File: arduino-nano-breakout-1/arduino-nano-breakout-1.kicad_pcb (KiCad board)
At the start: 2 copper layers, 7 x 7 mm, 4 parts, among them J1 PJ-002A, J2 Conn_01x03_Male, J4 Conn_01x08_Male

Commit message: move
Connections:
- J4 pad 2: Net-(A1-Pad27) -> Net-(J1-Pad1)
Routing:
- net Net-(J1-Pad1): track 14.5 -> 51.3 mm
- net GND: track 65.4 -> 80.5 mm, vias 1 -> 2
- net Net-(A1-Pad27): track 42.7 -> 48.2 mm
- net Net-(A1-Pad30): track 52.1 -> 55.2 mm

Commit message: final piece?
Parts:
- added JP1: SolderJumper_3_Open, Jumper:SolderJumper-3_P1.3mm_Open_Pad1.0x1.5mm, F.Cu at (134.6, 77.5)
- added JP2: SolderJumper_3_Open, Jumper:SolderJumper-3_P1.3mm_Open_Pad1.0x1.5mm, F.Cu at (134.6, 85.1)
- added JP3: SolderJumper_3_Open, Jumper:SolderJumper-3_P1.3mm_Open_Pad1.0x1.5mm, F.Cu at (134.6, 92.7)
- added JP4: SolderJumper_3_Open, Jumper:SolderJumper-3_P1.3mm_Open_Pad1.0x1.5mm, F.Cu at (134.6, 100.3)
- J1: footprint CUI_PJ-002A -> SS_connectors:CUI_PJ-002A
- moved J4 2.29 mm to (157.5, 79.4)
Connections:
- A1 pad 1: Net-(A1-Pad1) -> (no net)
- A1 pad 10: Net-(A1-Pad10) -> (no net)
- A1 pad 11: Net-(A1-Pad11) -> (no net)
- A1 pad 14: Net-(A1-Pad14) -> (no net)
- A1 pad 15: Net-(A1-Pad15) -> (no net)
- A1 pad 16: Net-(A1-Pad16) -> (no net)
- A1 pad 17: Net-(A1-Pad17) -> (no net)
- A1 pad 18: Net-(A1-Pad18) -> (no net)
- A1 pad 19: Net-(A1-Pad19) -> (no net)
- A1 pad 2: Net-(A1-Pad2) -> (no net)
- A1 pad 20: Net-(A1-Pad20) -> (no net)
- A1 pad 23: Net-(A1-Pad23) -> (no net)
- A1 pad 26: Net-(A1-Pad26) -> (no net)
- A1 pad 28: Net-(A1-Pad28) -> (no net)
- A1 pad 3: Net-(A1-Pad3) -> (no net)
- A1 pad 7: Net-(A1-Pad7) -> (no net)
- J1 pad 3: Net-(J1-Pad3) -> (no net)
- J4 pad 1: GND -> Net-(J4-Pad1)
- J4 pad 2: Net-(J1-Pad1) -> Net-(J4-Pad2)
- J4 pad 3: IO2 -> Net-(J4-Pad3)
- J4 pad 4: IO3 -> Net-(J4-Pad4)
- J4 pad 5: IO5 -> IO9
- J4 pad 6: IO6 -> IO10
- J4 pad 7: IO9 -> GND
- J4 pad 8: IO10 -> Net-(J1-Pad1)
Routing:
- net GND: track 80.5 -> 18.9 mm, vias 2 -> 4
- net Net-(J1-Pad1): track 51.3 -> 15.4 mm, vias 0 -> 2
- net Net-(A1-Pad21): track 0.00 -> 31.5 mm, vias 0 -> 1
- net Net-(J4-Pad4): track 0.00 -> 30.2 mm, vias 0 -> 1
- net Net-(J4-Pad3): track 0.00 -> 26.3 mm, vias 0 -> 1
- net Net-(J4-Pad1): track 0.00 -> 26.2 mm, vias 0 -> 1
- net IO5: track 29.3 -> 5.09 mm, vias 0 -> 1
- net Net-(J4-Pad2): track 0.00 -> 24.2 mm, vias 0 -> 1
- net Net-(A1-Pad25): track 0.00 -> 23.7 mm, vias 0 -> 1
- net Net-(A1-Pad22): track 0.00 -> 22.5 mm, vias 0 -> 1
- net IO3: track 28.2 -> 6.52 mm, vias 0 -> 1
- net IO6: track 29.3 -> 8.31 mm, vias 0 -> 1
- net Net-(A1-Pad27): track 48.2 -> 31.4 mm
- net IO2: track 28.2 -> 11.5 mm, vias 0 -> 1
- net Net-(A1-Pad30): track 55.2 -> 44.5 mm
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- added copper zone on B.Cu, net GND
- added copper zone on B.Cu, net Net-(J1-Pad1)
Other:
- board size 7 x 7 mm -> 37.5 x 48.9 mm

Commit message: VDD filtering capacitors
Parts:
- added C1: 100nF, Capacitor_SMD:C_0805_2012Metric, F.Cu at (148.3, 77.5)
- added C2: 100nF, Capacitor_SMD:C_0805_2012Metric, F.Cu at (149.2, 81.6)
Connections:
- A1 pad 1: (no net) -> Net-(A1-Pad1)
- A1 pad 10: (no net) -> Net-(A1-Pad10)
- A1 pad 11: (no net) -> Net-(A1-Pad11)
- A1 pad 14: (no net) -> Net-(A1-Pad14)
- A1 pad 15: (no net) -> Net-(A1-Pad15)
- A1 pad 16: (no net) -> Net-(A1-Pad16)
- A1 pad 17: (no net) -> Net-(A1-Pad17)
- A1 pad 18: (no net) -> Net-(A1-Pad18)
- A1 pad 19: (no net) -> Net-(A1-Pad19)
- A1 pad 2: (no net) -> Net-(A1-Pad2)
- A1 pad 20: (no net) -> Net-(A1-Pad20)
- A1 pad 23: (no net) -> Net-(A1-Pad23)
- A1 pad 26: (no net) -> Net-(A1-Pad26)
- A1 pad 28: (no net) -> Net-(A1-Pad28)
- A1 pad 3: (no net) -> Net-(A1-Pad3)
- A1 pad 7: (no net) -> Net-(A1-Pad7)
- J1 pad 3: (no net) -> Net-(J1-Pad3)
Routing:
- net GND: track 18.9 -> 21.5 mm, vias 4 -> 6
- net Net-(A1-Pad27): track 31.4 -> 32.7 mm

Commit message: Add silks
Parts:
- moved C2 1.82 mm to (150.5, 82.9)
- renumbered JP1 to IO_2, JP2 to IO_3, JP3 to IO_5, JP4 to IO_6
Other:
- board text added: "A2"
- board text added: "A3"
- board text added: "A5"
- board text added: "A6"
- board text added: "D2"
- board text added: "D3"
- board text added: "D5"
- board text added: "D6"
- board text added: "GND"
- board text added: "IO_10"
- board text added: "IO_2"
- board text added: "IO_3"
- board text added: "IO_5"
- board text added: "IO_6"
- board text added: "IO_9"
- board text added: "Vout"
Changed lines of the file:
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@@
   (general
     (thickness 1.6)
-    (drawings 4)
-    (tracks 149)
+    (drawings 20)
+    (tracks 150)
     (zones 0)
     (modules 10)
@@
     (tags "solder jumper open")
     (attr virtual)
-    (fp_text reference JP1 (at 0 -1.8 270) (layer F.SilkS)
+    (fp_text reference IO_2 (at 0 -1.8 270) (layer F.SilkS)
       (effects (font (size 1 1) (thickness 0.15)))
     )
@@
     (tags "solder jumper open")
     (attr virtual)
-    (fp_text reference JP2 (at 0 -1.8 270) (layer F.SilkS)
+    (fp_text reference IO_3 (at 0 -1.8 270) (layer F.SilkS)
       (effects (font (size 1 1) (thickness 0.15)))
     )
@@
     (tags "solder jumper open")
     (attr virtual)
-    (fp_text reference JP3 (at 0 -1.8 270) (layer F.SilkS)
+    (fp_text reference IO_5 (at 0 -1.8 270) (layer F.SilkS)
       (effects (font (size 1 1) (thickness 0.15)))
     )
@@
     (tags "solder jumper open")
     (attr virtual)
-    (fp_text reference JP4 (at 0 -1.8 270) (layer F.SilkS)
+    (fp_text reference IO_6 (at 0 -1.8 270) (layer F.SilkS)
       (effects (font (size 1 1) (thickness 0.15)))
     )
@@
   )
   (module Capacitor_SMD:C_0805_2012Metric (layer F.Cu)
-    (at 149.225 81.5825 90)
+    (at 150.495 82.8825 90)
     (descr "Capacitor SMD 0805 (2012 Metric), square (rectangular) end terminal, IPC_7351 nominal, (Body size source: https://docs.google.com/spreadsheets/d/1BsfQQcO9C6DZCsRaXUlFlo91Tg2WpOkGARC1WS5S8t0/edit?usp=sharing), generated with kicad-footprint-generator")
     (tags capacitor)
@@
       (rotate (xyz 0 0 0))
     )
+  )
+  (gr_text Vout (at 153.035 97.79) (layer F.SilkS)
+    (effects (font (size 1.5 1.5) (thickness 0.3)))
+  )
+  (gr_text GND (at 153.035 94.615) (layer F.SilkS)
+    (effects (font (size 1.5 1.5) (thickness 0.3)))
+  )
+  (gr_text IO_10 (at 153.67 92.075) (layer F.SilkS)
+    (effects (font (size 0.8 0.8) (thickness 0.125)))
+  )
+  (gr_text IO_9 (at 153.67 89.535) (layer F.SilkS)
+    (effects (font (size 0.8 0.8) (thickness 0.125)))
+  )
+  (gr_text IO_6 (at 153.67 86.995) (layer F.SilkS)
+    (effects (font (size 0.8 0.8) (thickness 0.125)))
+  )
+  (gr_text IO_5 (at 153.67 84.455) (layer F.SilkS)
+    (effects (font (size 0.8 0.8) (thickness 0.125)))
+  )
+  (gr_text IO_3 (at 153.67 81.915) (layer F.SilkS)
+    (effects (font (size 0.8 0.8) (thickness 0.125)))
+  )
+  (gr_text IO_2 (at 153.67 79.375) (layer F.SilkS)
+    (effects (font (size 0.8 0.8) (thickness 0.125)))
+  )
+  (gr_text D3 (at 132.08 86.995 90) (layer F.SilkS)
+    (effects (font (size 1.5 1.5) (thickness 0.3)))
+  )
+  (gr_text D2 (at 132.08 79.375 90) (layer F.SilkS)
+    (effects (font (size 1.5 1.5) (thickness 0.3)))
+  )
+  (gr_text D5 (at 132.08 94.615 90) (layer F.SilkS)
+    (effects (font (size 1.5 1.5) (thickness 0.3)))
+  )
+  (gr_text D6 (at 132.08 102.235 90) (layer F.SilkS)
+    (effects (font (size 1.5 1.5) (thickness 0.3)))
+  )
+  (gr_text A2 (at 132.08 75.565 90) (layer F.SilkS)
+    (effects (font (size 1.5 1.5) (thickness 0.3)))
+  )
+  (gr_text A3 (at 132.08 83.185 90) (layer F.SilkS)
+    (effects (font (size 1.5 1.5) (thickness 0.3)))
+  )
+  (gr_text A6 (at 132.08 98.425 90) (layer F.SilkS)
+    (effects (font (size 1.5 1.5) (thickness 0.3)))
+  )
+  (gr_text A5 (at 132.08 90.805 90) (layer F.SilkS)
+    (effects (font (size 1.5 1.5) (thickness 0.3)))
   )
   (gr_line (start 127 70.485) (end 164.465 70.485) (layer Edge.Cuts) (width 0.15))
@@
   (segment (start 150.495 77.47) (end 149.195 77.47) (width 1) (layer F.Cu) (net 1))
   (via (at 150.495 80.645) (size 0.8) (drill 0.4) (layers F.Cu B.Cu) (net 1))
-  (segment (start 149.225 80.645) (end 150.495 80.645) (width 1) (layer F.Cu) (net 1))
+  (segment (start 150.495 81.945) (end 150.495 80.645) (width 1) (layer F.Cu) (net 1))
   (segment (start 144.78 99.06) (end 142.875 99.06) (width 0.25) (layer B.Cu) (net 2))
   (segment (start 142.875 99.06) (end 142.875 99.06) (width 0.25) (layer B.Cu) (net 2))
@@
   (segment (start 144.78 83.82) (end 149.225 83.82) (width 1) (layer B.Cu) (net 6))
   (segment (start 149.86 107.95) (end 149.225 107.315) (width 1) (layer F.Cu) (net 6))
-  (segment (start 149.225 107.315) (end 149.225 84.385685) (width 1) (layer F.Cu) (net 6))
-  (segment (start 149.225 84.385685) (end 149.225 83.82) (width 1) (layer F.Cu) (net 6))
-  (segment (start 149.225 83.82) (end 149.225 82.52) (width 1) (layer F.Cu) (net 6))
+  (segment (start 149.225 83.82) (end 150.495 83.82) (width 1) (layer F.Cu) (net 6))
+  (segment (start 149.225 107.315) (end 149.225 86.995) (width 1) (layer F.Cu) (net 6))
+  (segment (start 149.225 86.995) (end 150.495 85.725) (width 1) (layer F.Cu) (net 6))
+  (segment (start 150.495 85.725) (end 150.495 83.82) (width 1) (layer F.Cu) (net 6))
   (segment (start 149.86 115.57) (end 147.32 115.57) (width 1) (layer B.Cu) (net 7))
   (segment (start 147.32 115.57) (end 147.32 115.57) (width 1) (layer B.Cu) (net 7))

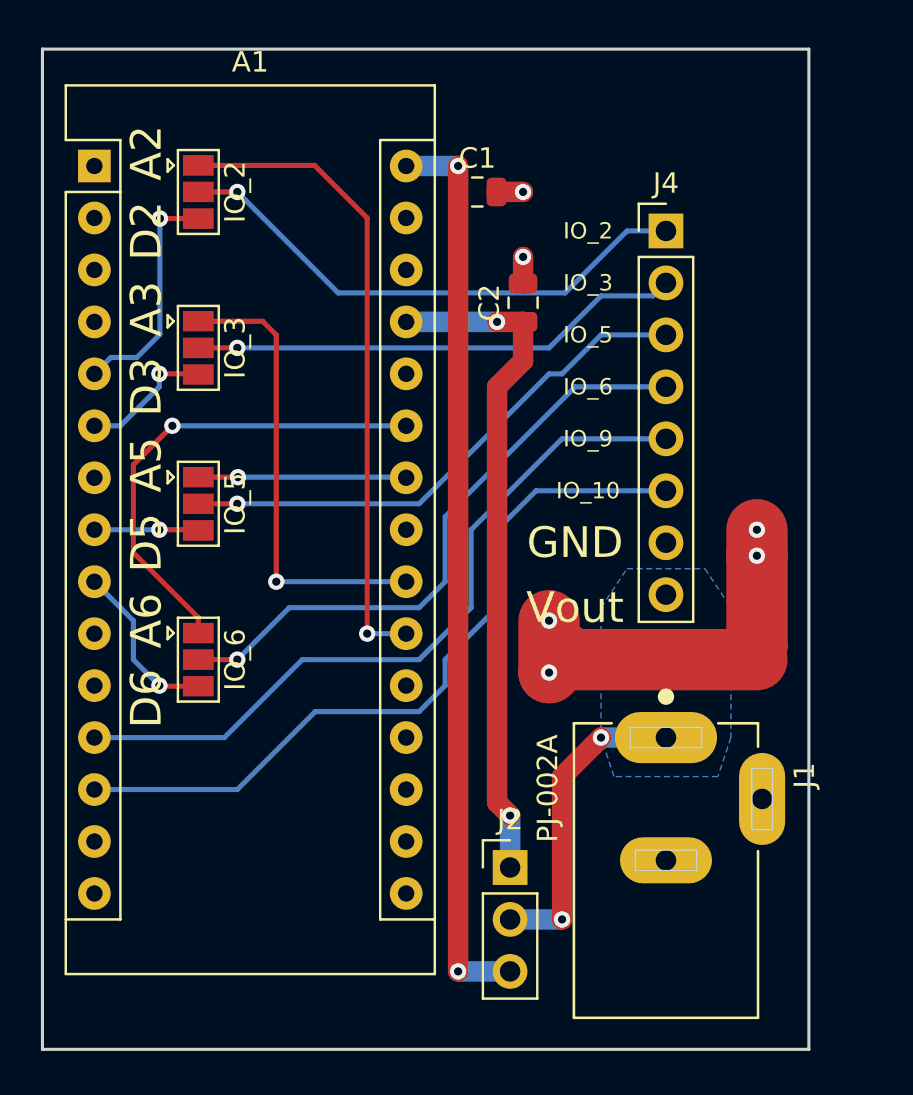
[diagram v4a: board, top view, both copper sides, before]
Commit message: change power connector
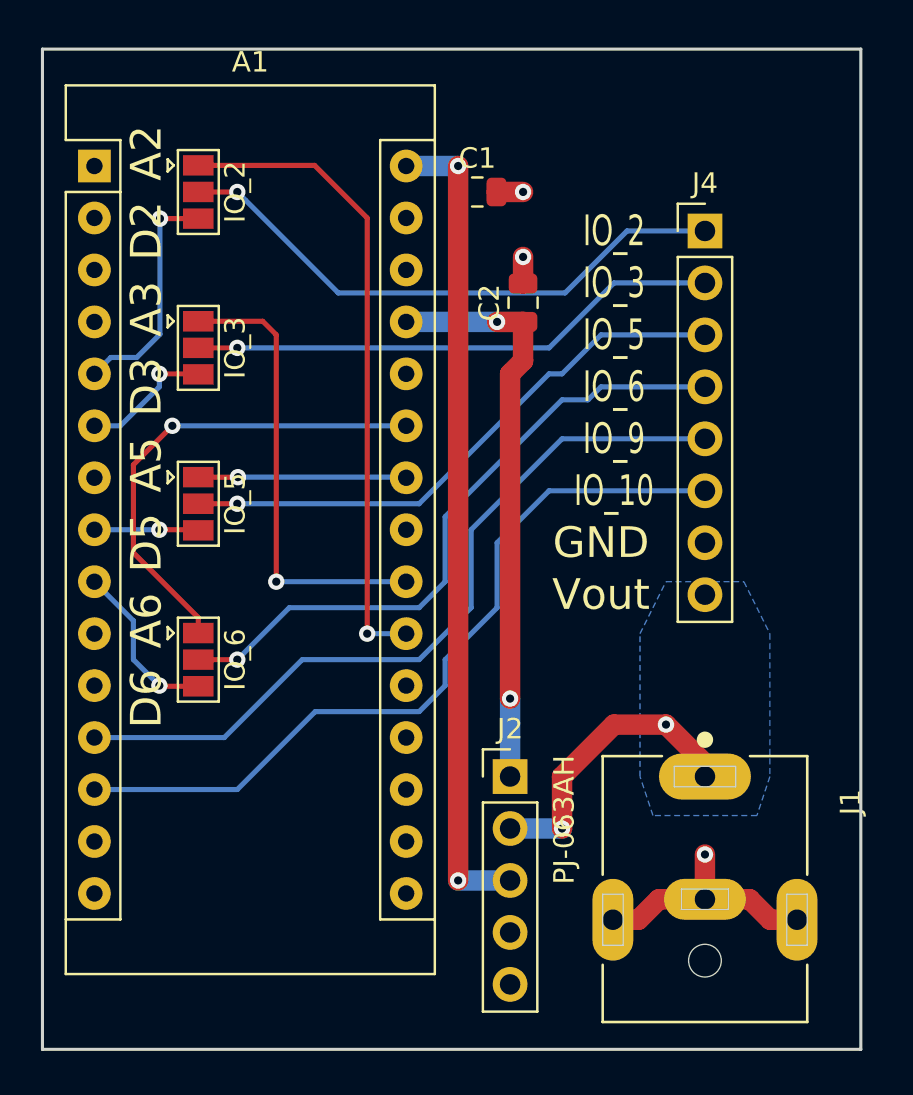
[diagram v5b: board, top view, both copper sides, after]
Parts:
- J1: value PJ-002A -> PJ-063AH; footprint SS_connectors:CUI_PJ-002A -> CUI_PJ-063AH
- J2: value Conn_01x03_Male -> Conn_01x05_Male; footprint Connector_PinHeader_2.54mm:PinHeader_1x03_P2.54mm_Vertical -> Connector_PinHeader_2.54mm:PinHeader_1x05_P2.54mm_Vertical
- moved J2 4.44 mm to (149.9, 106.0)
- moved J1 2.69 mm to (159.4, 106.0)
- moved J4 1.91 mm to (159.4, 79.4)
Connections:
- net IO10 renamed D10
- net IO2 renamed D2
- net IO3 renamed D3
- net IO5 renamed D5
- net IO6 renamed D6
- net IO9 renamed D9
- A1 pad 1: Net-(A1-Pad1) -> (no net)
- A1 pad 10: Net-(A1-Pad10) -> (no net)
- A1 pad 11: Net-(A1-Pad11) -> (no net)
- A1 pad 14: Net-(A1-Pad14) -> (no net)
- A1 pad 15: Net-(A1-Pad15) -> (no net)
- A1 pad 16: Net-(A1-Pad16) -> (no net)
- A1 pad 17: Net-(A1-Pad17) -> (no net)
- A1 pad 18: Net-(A1-Pad18) -> (no net)
- A1 pad 19: Net-(A1-Pad19) -> (no net)
- A1 pad 2: Net-(A1-Pad2) -> (no net)
- A1 pad 20: Net-(A1-Pad20) -> (no net)
- A1 pad 23: Net-(A1-Pad23) -> (no net)
- A1 pad 26: Net-(A1-Pad26) -> (no net)
- A1 pad 28: Net-(A1-Pad28) -> (no net)
- A1 pad 3: Net-(A1-Pad3) -> (no net)
- A1 pad 7: Net-(A1-Pad7) -> (no net)
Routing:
- net GND: track 21.5 -> 14.6 mm, vias 6 -> 3
- net Net-(A1-Pad27): track 33.2 -> 28.2 mm
- net Net-(A1-Pad30): track 44.5 -> 40.0 mm
- net Net-(IO_5-Pad2): track 26.3 -> 28.2 mm
- net Net-(IO_3-Pad2): track 24.2 -> 26.1 mm
- net Net-(IO_2-Pad2): track 26.2 -> 28.1 mm
- net D9: track 36.2 -> 38.1 mm
- net Net-(IO_6-Pad2): track 30.2 -> 32.1 mm
- net D10: track 37.0 -> 38.5 mm
- net Net-(J1-Pad1): track 15.4 -> 14.5 mm
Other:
- board size 37.5 x 48.9 mm -> 40 x 48.9 mm

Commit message: tweaks
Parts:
- removed J4: Conn_01x08_Male, Connector_PinHeader_2.54mm:PinHeader_1x08_P2.54mm_Vertical
- added J3: Conn_01x10_Male, Connector_PinHeader_2.54mm:PinHeader_1x10_P2.54mm_Vertical, F.Cu at (160.7, 99.1)
- moved J2 10.2 mm to (149.9, 116.2), turned to 180 degrees
- renumbered IO_2 to IO2, IO_3 to IO3, IO_5 to IO5, IO_6 to IO6
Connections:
- A1 pad 1: (no net) -> D1
- A1 pad 10: (no net) -> Net-(A1-Pad10)
- A1 pad 11: (no net) -> Net-(A1-Pad11)
- A1 pad 14: (no net) -> Net-(A1-Pad14)
- A1 pad 15: (no net) -> Net-(A1-Pad15)
- A1 pad 16: (no net) -> Net-(A1-Pad16)
- A1 pad 17: (no net) -> Net-(A1-Pad17)
- A1 pad 18: (no net) -> Net-(A1-Pad18)
- A1 pad 19: (no net) -> Net-(A1-Pad19)
- A1 pad 2: (no net) -> D0
- A1 pad 20: (no net) -> Net-(A1-Pad20)
- A1 pad 23: (no net) -> Net-(A1-Pad23)
- A1 pad 26: (no net) -> Net-(A1-Pad26)
- A1 pad 28: (no net) -> Net-(A1-Pad28)
- A1 pad 3: (no net) -> Net-(A1-Pad3)
- A1 pad 7: (no net) -> Net-(A1-Pad7)
- J2 pad 1: Net-(A1-Pad27) -> GND
- J2 pad 2: Net-(J1-Pad1) -> Net-(J2-Pad2)
- J2 pad 4: (no net) -> Net-(J1-Pad1)
- J2 pad 5: GND -> Net-(A1-Pad27)
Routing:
- net D1: track 0.00 -> 40.5 mm, vias 0 -> 2
- net D0: track 0.00 -> 34.5 mm, vias 0 -> 2
- net Net-(A1-Pad25): track 23.7 -> 18.1 mm
- net Net-(IO_2-Pad2): track 28.1 -> 31.4 mm
- net Net-(IO_3-Pad2): track 26.1 -> 29.3 mm
- net D6: track 8.31 -> 10.1 mm
- net D5: track 5.09 -> 6.12 mm
- net Net-(A1-Pad22): track 22.5 -> 21.8 mm
- net D2: track 11.5 -> 10.8 mm
- net D10: track 38.5 -> 37.9 mm
- net D9: track 38.1 -> 37.5 mm
- net Net-(IO_6-Pad2): track 32.1 -> 31.5 mm
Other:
- board text added: "D0/Rx"
- board text added: "D1/Tx"
- board text added: "D10"
- board text added: "D9"
- board text added: "IO2"
- board text added: "IO3"
- board text added: "IO5"
- board text added: "IO6"
- board text added: "Sami Sorell"
- board text added: "Tiny Arduino Breakout Board 1"
- board text removed: "IO_10"
- board text removed: "IO_2"
- board text removed: "IO_3"
- board text removed: "IO_5"
- board text removed: "IO_6"
- board text removed: "IO_9"

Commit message: ground fill and vias
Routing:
- net GND: track 14.3 -> 12.0 mm, vias 3 -> 53
- net Net-(A1-Pad25): track 18.1 -> 19.1 mm
- net Net-(A1-Pad22): track 21.8 -> 22.7 mm
- net D3: track 6.85 -> 6.12 mm
- net D1: track 40.5 -> 39.9 mm
- added copper zone on F.Cu, net GND
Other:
- board text added: "Tiny Arduino Breakout Board"
- board text removed: "Tiny Arduino Breakout Board 1"

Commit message: tweak
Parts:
- J1: footprint CUI_PJ-063AH -> SS_connectors:CUI_PJ-063AH-1
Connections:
- A1 pad 10: Net-(A1-Pad10) -> (no net)
- A1 pad 11: Net-(A1-Pad11) -> (no net)
- A1 pad 14: Net-(A1-Pad14) -> (no net)
- A1 pad 15: Net-(A1-Pad15) -> (no net)
- A1 pad 16: Net-(A1-Pad16) -> (no net)
- A1 pad 17: Net-(A1-Pad17) -> (no net)
- A1 pad 18: Net-(A1-Pad18) -> (no net)
- A1 pad 19: Net-(A1-Pad19) -> (no net)
- A1 pad 20: Net-(A1-Pad20) -> (no net)
- A1 pad 23: Net-(A1-Pad23) -> (no net)
- A1 pad 26: Net-(A1-Pad26) -> (no net)
- A1 pad 28: Net-(A1-Pad28) -> (no net)
- A1 pad 3: Net-(A1-Pad3) -> (no net)
- A1 pad 7: Net-(A1-Pad7) -> (no net)
- J2 pad 2: Net-(J2-Pad2) -> (no net)
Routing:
- net GND: vias 53 -> 49
- net (no net): vias 0 -> 1
